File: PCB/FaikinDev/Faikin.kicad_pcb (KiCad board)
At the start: 2 copper layers, 70 x 70 mm, 32 parts, among them J1 1x5, J2 TC2030-USB-NL, J3 Reset, Q1 BSS138PS, U1 TPS562243, U4 ESP32-S3-MINI-1

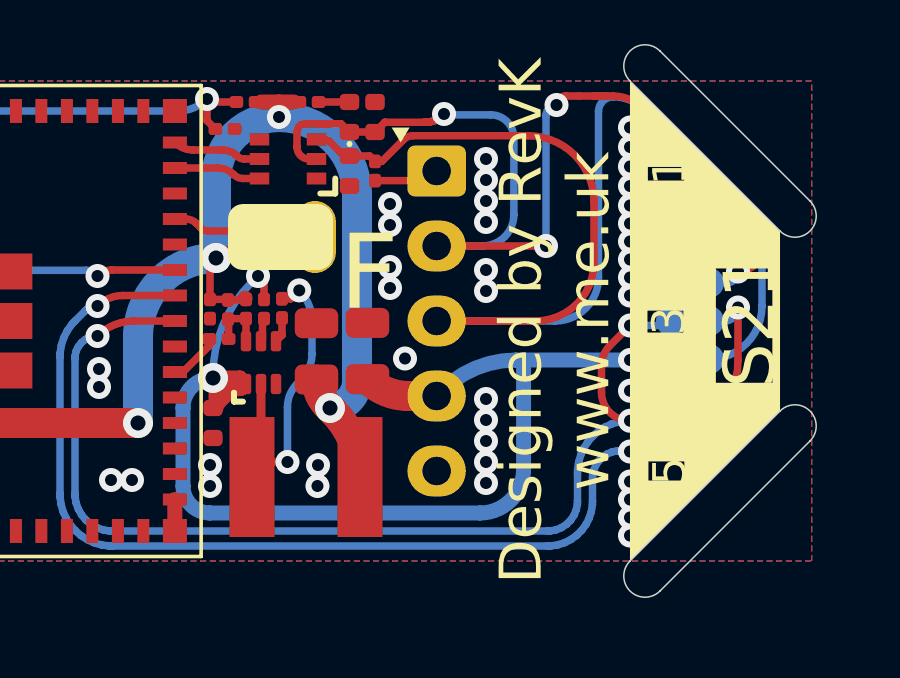
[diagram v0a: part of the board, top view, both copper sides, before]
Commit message: Moved caps away from heat
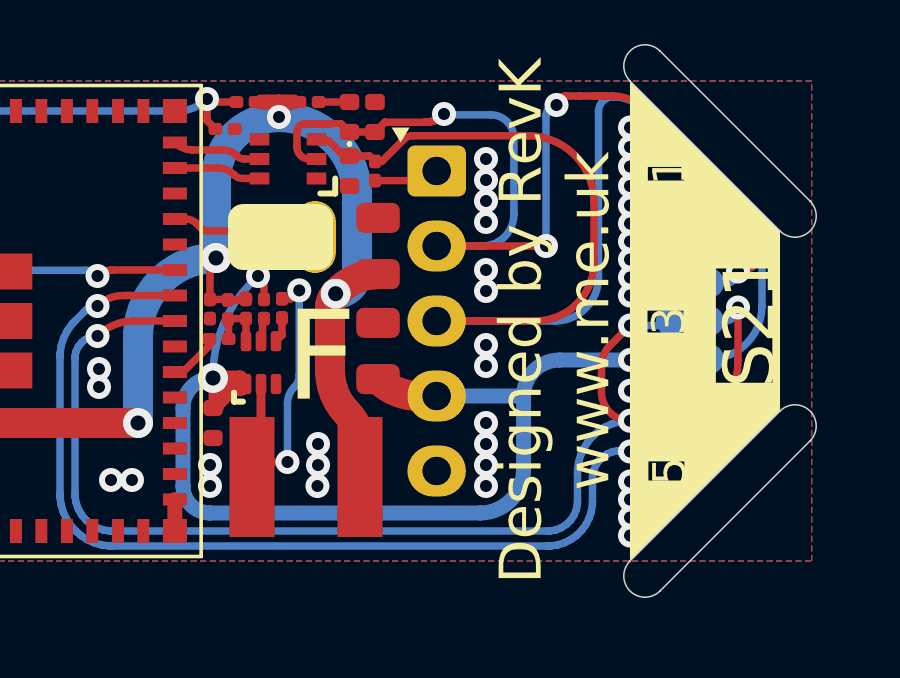
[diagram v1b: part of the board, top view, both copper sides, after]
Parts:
- U1: value TPS562243 -> TPS562246
- moved C15 4.07 mm to (143.6, 62.5)
- moved C17 0.35 mm to (143.6, 66.0)
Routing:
- net DC: track 39.0 -> 38.0 mm
- net GND: vias 51 -> 48

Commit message: PCB tweak
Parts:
- added C2: 100nF, RevK:C_0201, F.Cu at (141.4, 66.0)
- added C3: 100nF, RevK:C_0201, F.Cu at (141.4, 67.1)
- added C4: 100nF, RevK:C_0201, F.Cu at (141.4, 64.9)
- moved C6 0.32 mm to (138.6, 58.3)
- moved C15 0.30 mm to (143.6, 62.2)
- moved R1 0.20 mm to (143.5, 59.8)
- moved C16 0.10 mm to (138.1, 68.5)
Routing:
- net SW: track 10.2 -> 13.3 mm
- net GND: track 2.51 -> 5.27 mm, vias 48 -> 50
- net DC: track 38.0 -> 35.9 mm

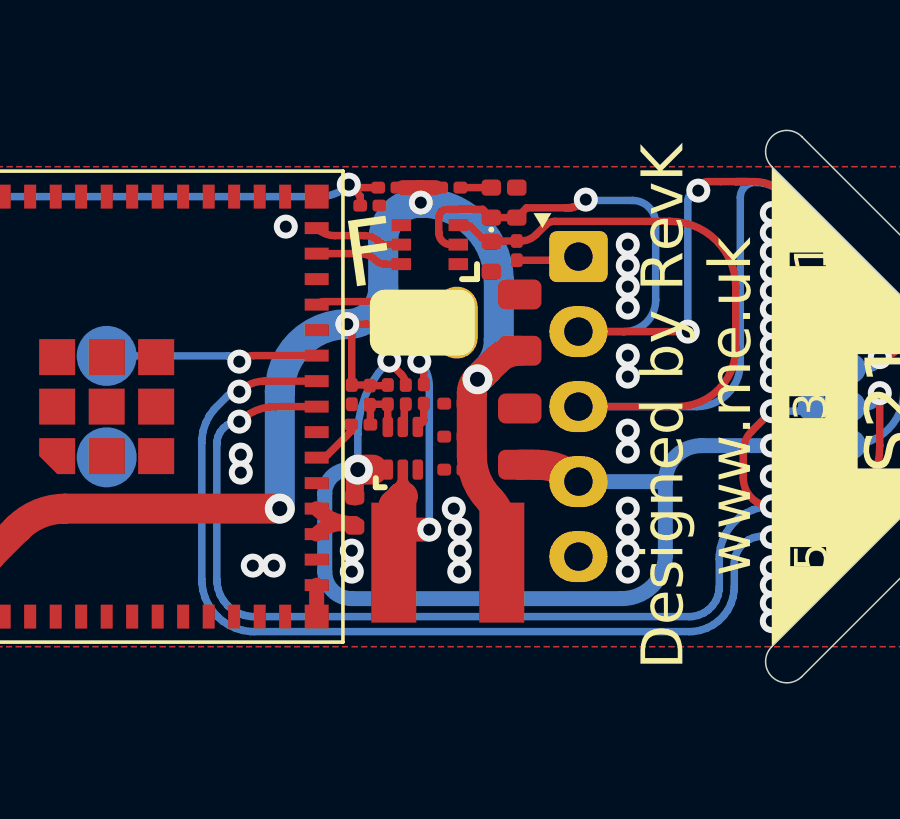
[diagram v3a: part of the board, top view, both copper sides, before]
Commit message: Tweak caps and inductor
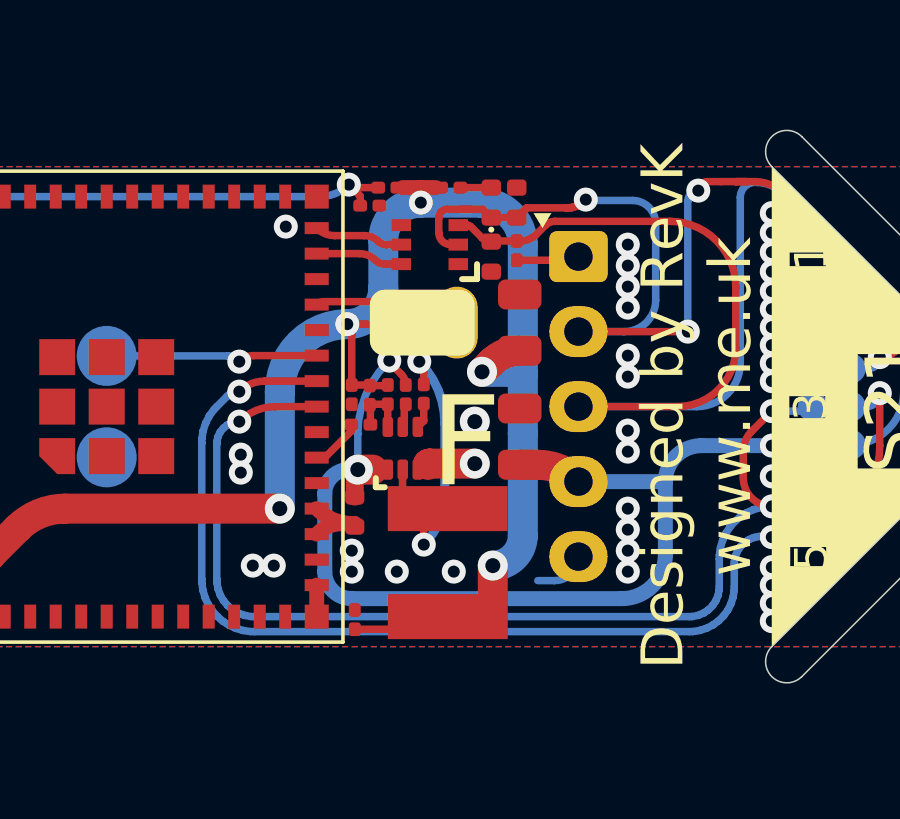
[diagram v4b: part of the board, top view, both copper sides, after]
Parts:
- removed C3, C4: 100nF, RevK:C_0201
- moved C2 6.94 mm to (138.1, 72.1), turned to -90 degrees
- turned L1 to -90 degrees
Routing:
- net +3.3V: track 47.4 -> 55.5 mm, vias 4 -> 5
- net GND: track 5.27 -> 8.63 mm
- net SW: track 13.3 -> 11.7 mm

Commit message: You can never have too many caps.
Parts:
- added C3: 100nF 25V, RevK:C_0402, F.Cu at (144.3, 68.7)
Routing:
- net GND: track 8.63 -> 10.2 mm
- net DC: track 35.9 -> 37.5 mm

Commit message: FFS
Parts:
- added C4: 100nF, RevK:C_0201, F.Cu at (144.2, 70.7)
- added C5: 100nF, RevK:C_0201, F.Cu at (143.6, 64.1)
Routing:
- net +3.3V: track 55.5 -> 58.3 mm
- net SW: track 11.7 -> 13.1 mm
- net GND: vias 50 -> 52
